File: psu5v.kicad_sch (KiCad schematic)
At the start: 26 parts, among them U16 AP64501SP-13

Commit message: work on control logic
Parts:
- renumbered C50 to C52, C51 to C53, C52 to C54, C53 to C55, C54 to C56, C55 to C57, C56 to C58, C57 to C59, C58 to C60, C59 to C61, C60 to C62, C61 to C63, C62 to C64, C63 to C65, C64 to C66, C65 to C67, R61 to R64, R62 to R65, R63 to R66, R64 to R67, R65 to R68, U16 to U17
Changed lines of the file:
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@@
   (symbol (lib_id "power:GND") (at 152.4 148.59 0) (unit 1)
     (in_bom yes) (on_board yes)
-    (property "Reference" "#PWR049" (id 0) (at 152.4 154.94 0)
+    (property "Reference" "#PWR050" (id 0) (at 152.4 154.94 0)
       (effects (font (size 1.27 1.27)) hide)
     )
@@
   (symbol (lib_id "Device:C_Small") (at 259.08 111.76 0) (unit 1)
     (in_bom yes) (on_board yes)
-    (property "Reference" "C62" (id 0) (at 261.62 110.49 0)
+    (property "Reference" "C64" (id 0) (at 261.62 110.49 0)
       (effects (font (size 1.27 1.27)) (justify left))
     )
@@
   (symbol (lib_id "Device:R_Small") (at 226.06 137.16 0) (unit 1)
     (in_bom yes) (on_board yes)
-    (property "Reference" "R64" (id 0) (at 227.33 135.89 0)
+    (property "Reference" "R67" (id 0) (at 227.33 135.89 0)
       (effects (font (size 1.27 1.27)) (justify left))
     )
@@
   (symbol (lib_id "Device:R_Small") (at 219.71 118.11 0) (unit 1)
     (in_bom yes) (on_board yes)
-    (property "Reference" "R63" (id 0) (at 220.98 116.84 0)
+    (property "Reference" "R66" (id 0) (at 220.98 116.84 0)
       (effects (font (size 1.27 1.27)) (justify left))
     )
@@
   (symbol (lib_id "Device:C_Small") (at 232.41 118.11 0) (unit 1)
     (in_bom no) (on_board no)
-    (property "Reference" "C60" (id 0) (at 234.95 116.84 0)
+    (property "Reference" "C62" (id 0) (at 234.95 116.84 0)
       (effects (font (size 1.27 1.27)) (justify left))
     )
@@
   (symbol (lib_id "Device:C_Small") (at 213.36 140.97 0) (unit 1)
     (in_bom yes) (on_board yes)
-    (property "Reference" "C59" (id 0) (at 215.9 139.7 0)
+    (property "Reference" "C61" (id 0) (at 215.9 139.7 0)
       (effects (font (size 1.27 1.27)) (justify left))
     )
@@
   (symbol (lib_id "Device:R_Small") (at 306.705 112.395 0) (unit 1)
     (in_bom yes) (on_board yes)
-    (property "Reference" "R65" (id 0) (at 309.88 111.125 0))
+    (property "Reference" "R68" (id 0) (at 309.88 111.125 0))
     (property "Value" "1k" (id 1) (at 309.88 113.665 0))
     (property "Footprint" "Resistor_SMD:R_0402_1005Metric" (id 2) (at 306.705 112.395 0)
@@
   (symbol (lib_id "power:GND") (at 290.83 148.59 0) (unit 1)
     (in_bom yes) (on_board yes)
-    (property "Reference" "#PWR053" (id 0) (at 290.83 154.94 0)
+    (property "Reference" "#PWR054" (id 0) (at 290.83 154.94 0)
       (effects (font (size 1.27 1.27)) hide)
     )
@@
   (symbol (lib_id "Regulator_Switching_Diodes:AP64501SP-13") (at 182.88 124.46 0) (unit 1)
     (in_bom yes) (on_board yes)
-    (property "Reference" "U16" (id 0) (at 182.245 114.3 0))
+    (property "Reference" "U17" (id 0) (at 182.245 114.3 0))
     (property "Value" "AP64501SP-13" (id 1) (at 182.88 116.84 0))
     (property "Footprint" "Regulator_Switching_Diodes:SOIC-8-1EP_3.9x4.9mm_P1.27mm_EP2.95x4.9mm_Mask2.71x3.4mm_ThermalVias" (id 2) (at 182.88 149.86 0)
@@
   (symbol (lib_id "Device:C_Small") (at 248.92 111.76 0) (unit 1)
     (in_bom yes) (on_board yes)
-    (property "Reference" "C61" (id 0) (at 251.46 110.49 0)
+    (property "Reference" "C63" (id 0) (at 251.46 110.49 0)
       (effects (font (size 1.27 1.27)) (justify left))
     )
@@
   (symbol (lib_id "power:GND") (at 279.4 148.59 0) (unit 1)
     (in_bom yes) (on_board yes)
-    (property "Reference" "#PWR052" (id 0) (at 279.4 154.94 0)
+    (property "Reference" "#PWR053" (id 0) (at 279.4 154.94 0)
       (effects (font (size 1.27 1.27)) hide)
     )
@@
   (symbol (lib_id "Device:C_Small") (at 163.83 114.3 0) (unit 1)
     (in_bom yes) (on_board yes)
-    (property "Reference" "C56" (id 0) (at 166.37 113.03 0)
+    (property "Reference" "C58" (id 0) (at 166.37 113.03 0)
       (effects (font (size 1.27 1.27)) (justify left))
     )
@@
   (symbol (lib_id "Device:R_Small") (at 173.99 106.68 270) (unit 1)
     (in_bom yes) (on_board yes)
-    (property "Reference" "R61" (id 0) (at 172.72 104.14 90)
+    (property "Reference" "R64" (id 0) (at 172.72 104.14 90)
       (effects (font (size 1.27 1.27)) (justify left))
     )
@@
   (symbol (lib_id "Device:R_Small") (at 213.36 133.35 0) (unit 1)
     (in_bom yes) (on_board yes)
-    (property "Reference" "R62" (id 0) (at 215.9 132.08 0)
+    (property "Reference" "R65" (id 0) (at 215.9 132.08 0)
       (effects (font (size 1.27 1.27)) (justify left))
     )
@@
   (symbol (lib_id "Device:C_Small") (at 279.4 111.76 0) (unit 1)
     (in_bom yes) (on_board yes)
-    (property "Reference" "C64" (id 0) (at 281.94 110.49 0)
+    (property "Reference" "C66" (id 0) (at 281.94 110.49 0)
       (effects (font (size 1.27 1.27)) (justify left))
     )
@@
   (symbol (lib_id "Device:C_Small") (at 172.72 137.16 0) (unit 1)
     (in_bom yes) (on_board yes)
-    (property "Reference" "C57" (id 0) (at 175.26 135.89 0)
+    (property "Reference" "C59" (id 0) (at 175.26 135.89 0)
       (effects (font (size 1.27 1.27)) (justify left))
     )
@@
   (symbol (lib_id "power:GND") (at 226.06 148.59 0) (unit 1)
     (in_bom yes) (on_board yes)
-    (property "Reference" "#PWR050" (id 0) (at 226.06 154.94 0)
+    (property "Reference" "#PWR051" (id 0) (at 226.06 154.94 0)
       (effects (font (size 1.27 1.27)) hide)
     )
@@
   (symbol (lib_id "Device:C_Small") (at 152.4 128.27 0) (unit 1)
     (in_bom yes) (on_board yes)
-    (property "Reference" "C55" (id 0) (at 154.94 127 0)
+    (property "Reference" "C57" (id 0) (at 154.94 127 0)
       (effects (font (size 1.27 1.27)) (justify left))
     )
@@
   (symbol (lib_id "Device:C_Small") (at 91.44 128.27 0) (unit 1)
     (in_bom yes) (on_board yes)
-    (property "Reference" "C51" (id 0) (at 93.98 127 0)
+    (property "Reference" "C53" (id 0) (at 93.98 127 0)
       (effects (font (size 1.27 1.27)) (justify left))
     )
@@
   (symbol (lib_id "Device:C_Small") (at 269.24 111.76 0) (unit 1)
     (in_bom yes) (on_board yes)
-    (property "Reference" "C63" (id 0) (at 271.78 110.49 0)
+    (property "Reference" "C65" (id 0) (at 271.78 110.49 0)
       (effects (font (size 1.27 1.27)) (justify left))
     )
@@
   (symbol (lib_id "power:GND") (at 306.705 148.59 0) (unit 1)
     (in_bom yes) (on_board yes)
-    (property "Reference" "#PWR054" (id 0) (at 306.705 154.94 0)
+    (property "Reference" "#PWR055" (id 0) (at 306.705 154.94 0)
       (effects (font (size 1.27 1.27)) hide)
     )
@@
   (symbol (lib_id "Device:C_Small") (at 76.2 128.27 0) (unit 1)
     (in_bom yes) (on_board yes)
-    (property "Reference" "C50" (id 0) (at 78.74 127 0)
+    (property "Reference" "C52" (id 0) (at 78.74 127 0)
       (effects (font (size 1.27 1.27)) (justify left))
     )
@@
   (symbol (lib_id "power:GND") (at 251.46 142.24 0) (unit 1)
     (in_bom yes) (on_board yes)
-    (property "Reference" "#PWR051" (id 0) (at 251.46 148.59 0)
+    (property "Reference" "#PWR052" (id 0) (at 251.46 148.59 0)
       (effects (font (size 1.27 1.27)) hide)
     )
@@
   (symbol (lib_id "Capacitor_Tantalum_SMD_MyOwn:CP_EIA-7343-31_Kemet-D") (at 290.83 111.76 0) (unit 1)
     (in_bom yes) (on_board yes)
-    (property "Reference" "C65" (id 0) (at 293.37 110.49 0)
+    (property "Reference" "C67" (id 0) (at 293.37 110.49 0)
       (effects (font (size 1.27 1.27)) (justify left))
     )
@@
   (symbol (lib_id "Device:C_Small") (at 121.92 128.27 0) (unit 1)
     (in_bom yes) (on_board yes)
-    (property "Reference" "C53" (id 0) (at 124.46 127 0)
+    (property "Reference" "C55" (id 0) (at 124.46 127 0)
       (effects (font (size 1.27 1.27)) (justify left))
     )
@@
   (symbol (lib_id "Device:C_Small") (at 106.68 128.27 0) (unit 1)
     (in_bom yes) (on_board yes)
-    (property "Reference" "C52" (id 0) (at 109.22 127 0)
+    (property "Reference" "C54" (id 0) (at 109.22 127 0)
       (effects (font (size 1.27 1.27)) (justify left))
     )
@@
   (symbol (lib_id "Device:C_Small") (at 137.16 128.27 0) (unit 1)
     (in_bom yes) (on_board yes)
-    (property "Reference" "C54" (id 0) (at 139.7 127 0)
+    (property "Reference" "C56" (id 0) (at 139.7 127 0)
       (effects (font (size 1.27 1.27)) (justify left))
     )
@@
   (symbol (lib_id "Device:C_Small") (at 201.93 137.16 0) (unit 1)
     (in_bom yes) (on_board yes)
-    (property "Reference" "C58" (id 0) (at 204.47 135.89 0)
-      (effects (font (size 1.27 1.27)) (justify left))
-    )
+    (property "Reference" "C60" (id 0) (at 204.47 135.89 0)
+      (effects (font (size 1.27 1.27)) (justify left))
+    )

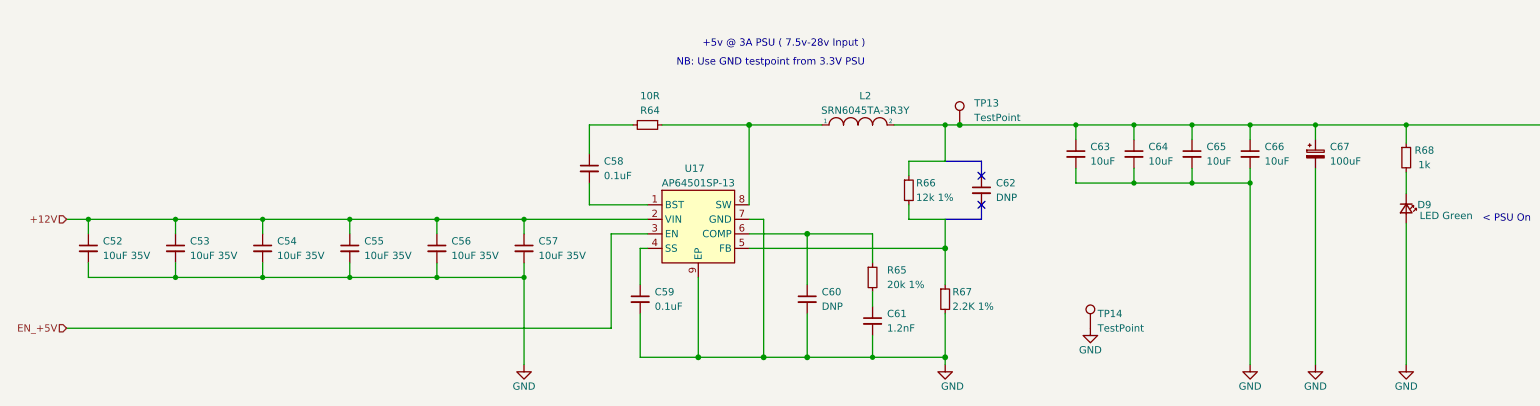
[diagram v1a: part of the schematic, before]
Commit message: connecterized faceplate, refreshed schematic
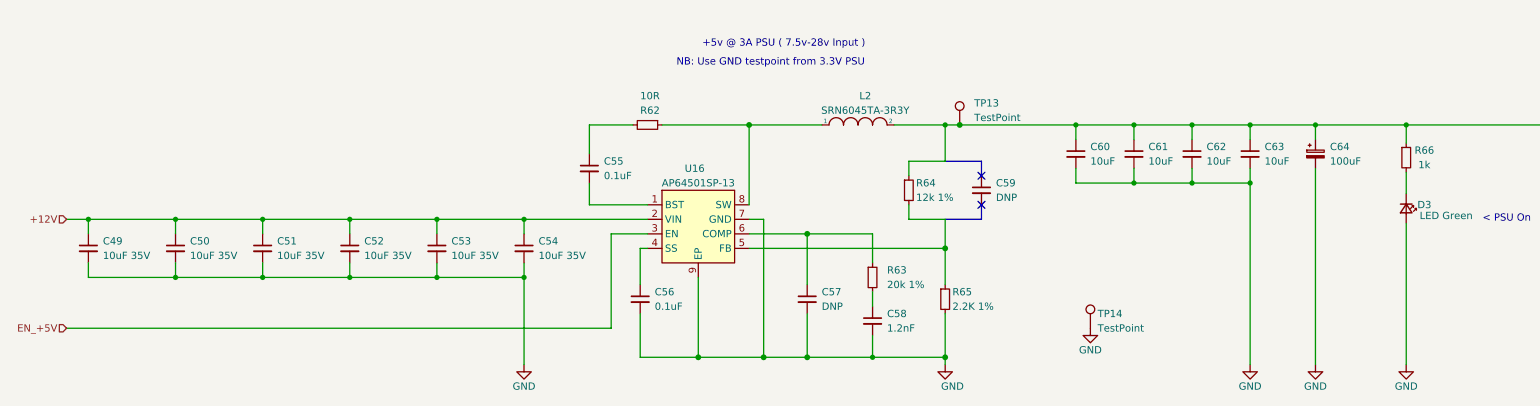
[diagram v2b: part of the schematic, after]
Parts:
- renumbered C52 to C49, C53 to C50, C54 to C51, C55 to C52, C56 to C53, C57 to C54, C58 to C55, C59 to C56, C60 to C57, C61 to C58, C62 to C59, C63 to C60, C64 to C61, C65 to C62, C66 to C63, C67 to C64, D9 to D3, R64 to R62, R65 to R63, R66 to R64, R67 to R65, R68 to R66, U17 to U16
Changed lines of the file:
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@@
   (symbol (lib_id "power:GND") (at 152.4 148.59 0) (unit 1)
     (in_bom yes) (on_board yes)
-    (property "Reference" "#PWR050" (id 0) (at 152.4 154.94 0)
+    (property "Reference" "#PWR049" (id 0) (at 152.4 154.94 0)
       (effects (font (size 1.27 1.27)) hide)
     )
@@
   (symbol (lib_id "Device:C_Small") (at 259.08 111.76 0) (unit 1)
     (in_bom yes) (on_board yes)
-    (property "Reference" "C64" (id 0) (at 261.62 110.49 0)
+    (property "Reference" "C61" (id 0) (at 261.62 110.49 0)
       (effects (font (size 1.27 1.27)) (justify left))
     )
@@
   (symbol (lib_id "Device:R_Small") (at 226.06 137.16 0) (unit 1)
     (in_bom yes) (on_board yes)
-    (property "Reference" "R67" (id 0) (at 227.33 135.89 0)
+    (property "Reference" "R65" (id 0) (at 227.33 135.89 0)
       (effects (font (size 1.27 1.27)) (justify left))
     )
@@
   (symbol (lib_id "Device:R_Small") (at 219.71 118.11 0) (unit 1)
     (in_bom yes) (on_board yes)
-    (property "Reference" "R66" (id 0) (at 220.98 116.84 0)
+    (property "Reference" "R64" (id 0) (at 220.98 116.84 0)
       (effects (font (size 1.27 1.27)) (justify left))
     )
@@
   (symbol (lib_id "Device:C_Small") (at 232.41 118.11 0) (unit 1)
     (in_bom no) (on_board no)
-    (property "Reference" "C62" (id 0) (at 234.95 116.84 0)
+    (property "Reference" "C59" (id 0) (at 234.95 116.84 0)
       (effects (font (size 1.27 1.27)) (justify left))
     )
@@
   (symbol (lib_id "Device:C_Small") (at 213.36 140.97 0) (unit 1)
     (in_bom yes) (on_board yes)
-    (property "Reference" "C61" (id 0) (at 215.9 139.7 0)
+    (property "Reference" "C58" (id 0) (at 215.9 139.7 0)
       (effects (font (size 1.27 1.27)) (justify left))
     )
@@
   (symbol (lib_id "Device:R_Small") (at 306.705 112.395 0) (unit 1)
     (in_bom yes) (on_board yes)
-    (property "Reference" "R68" (id 0) (at 309.88 111.125 0))
+    (property "Reference" "R66" (id 0) (at 309.88 111.125 0))
     (property "Value" "1k" (id 1) (at 309.88 113.665 0))
     (property "Footprint" "Resistor_SMD:R_0402_1005Metric" (id 2) (at 306.705 112.395 0)
@@
   (symbol (lib_id "power:GND") (at 290.83 148.59 0) (unit 1)
     (in_bom yes) (on_board yes)
-    (property "Reference" "#PWR054" (id 0) (at 290.83 154.94 0)
+    (property "Reference" "#PWR053" (id 0) (at 290.83 154.94 0)
       (effects (font (size 1.27 1.27)) hide)
     )
@@
   (symbol (lib_id "Regulator_Switching_Diodes:AP64501SP-13") (at 182.88 124.46 0) (unit 1)
     (in_bom yes) (on_board yes)
-    (property "Reference" "U17" (id 0) (at 182.245 114.3 0))
+    (property "Reference" "U16" (id 0) (at 182.245 114.3 0))
     (property "Value" "AP64501SP-13" (id 1) (at 182.88 116.84 0))
     (property "Footprint" "Regulator_Switching_Diodes:SOIC-8-1EP_3.9x4.9mm_P1.27mm_EP2.95x4.9mm_Mask2.71x3.4mm_ThermalVias" (id 2) (at 182.88 149.86 0)
@@
   (symbol (lib_id "Device:C_Small") (at 248.92 111.76 0) (unit 1)
     (in_bom yes) (on_board yes)
-    (property "Reference" "C63" (id 0) (at 251.46 110.49 0)
+    (property "Reference" "C60" (id 0) (at 251.46 110.49 0)
       (effects (font (size 1.27 1.27)) (justify left))
     )
@@
   (symbol (lib_id "power:GND") (at 279.4 148.59 0) (unit 1)
     (in_bom yes) (on_board yes)
-    (property "Reference" "#PWR053" (id 0) (at 279.4 154.94 0)
+    (property "Reference" "#PWR052" (id 0) (at 279.4 154.94 0)
       (effects (font (size 1.27 1.27)) hide)
     )
@@
   (symbol (lib_id "Device:C_Small") (at 163.83 114.3 0) (unit 1)
     (in_bom yes) (on_board yes)
-    (property "Reference" "C58" (id 0) (at 166.37 113.03 0)
+    (property "Reference" "C55" (id 0) (at 166.37 113.03 0)
       (effects (font (size 1.27 1.27)) (justify left))
     )
@@
   (symbol (lib_id "Device:R_Small") (at 173.99 106.68 270) (unit 1)
     (in_bom yes) (on_board yes)
-    (property "Reference" "R64" (id 0) (at 172.72 104.14 90)
+    (property "Reference" "R62" (id 0) (at 172.72 104.14 90)
       (effects (font (size 1.27 1.27)) (justify left))
     )
@@
   (symbol (lib_id "Device:R_Small") (at 213.36 133.35 0) (unit 1)
     (in_bom yes) (on_board yes)
-    (property "Reference" "R65" (id 0) (at 215.9 132.08 0)
+    (property "Reference" "R63" (id 0) (at 215.9 132.08 0)
       (effects (font (size 1.27 1.27)) (justify left))
     )
@@
   (symbol (lib_id "Device:C_Small") (at 279.4 111.76 0) (unit 1)
     (in_bom yes) (on_board yes)
-    (property "Reference" "C66" (id 0) (at 281.94 110.49 0)
+    (property "Reference" "C63" (id 0) (at 281.94 110.49 0)
       (effects (font (size 1.27 1.27)) (justify left))
     )
@@
   (symbol (lib_id "Device:C_Small") (at 172.72 137.16 0) (unit 1)
     (in_bom yes) (on_board yes)
-    (property "Reference" "C59" (id 0) (at 175.26 135.89 0)
+    (property "Reference" "C56" (id 0) (at 175.26 135.89 0)
       (effects (font (size 1.27 1.27)) (justify left))
     )
@@
   (symbol (lib_id "power:GND") (at 226.06 148.59 0) (unit 1)
     (in_bom yes) (on_board yes)
-    (property "Reference" "#PWR051" (id 0) (at 226.06 154.94 0)
+    (property "Reference" "#PWR050" (id 0) (at 226.06 154.94 0)
       (effects (font (size 1.27 1.27)) hide)
     )
@@
   (symbol (lib_id "Device:C_Small") (at 152.4 128.27 0) (unit 1)
     (in_bom yes) (on_board yes)
-    (property "Reference" "C57" (id 0) (at 154.94 127 0)
+    (property "Reference" "C54" (id 0) (at 154.94 127 0)
       (effects (font (size 1.27 1.27)) (justify left))
     )
@@
   (symbol (lib_id "Device:C_Small") (at 91.44 128.27 0) (unit 1)
     (in_bom yes) (on_board yes)
-    (property "Reference" "C53" (id 0) (at 93.98 127 0)
+    (property "Reference" "C50" (id 0) (at 93.98 127 0)
       (effects (font (size 1.27 1.27)) (justify left))
     )
@@
   (symbol (lib_id "Device:C_Small") (at 269.24 111.76 0) (unit 1)
     (in_bom yes) (on_board yes)
-    (property "Reference" "C65" (id 0) (at 271.78 110.49 0)
+    (property "Reference" "C62" (id 0) (at 271.78 110.49 0)
       (effects (font (size 1.27 1.27)) (justify left))
     )
@@
   (symbol (lib_id "power:GND") (at 306.705 148.59 0) (unit 1)
     (in_bom yes) (on_board yes)
-    (property "Reference" "#PWR055" (id 0) (at 306.705 154.94 0)
+    (property "Reference" "#PWR054" (id 0) (at 306.705 154.94 0)
       (effects (font (size 1.27 1.27)) hide)
     )
@@
   (symbol (lib_id "Device:C_Small") (at 76.2 128.27 0) (unit 1)
     (in_bom yes) (on_board yes)
-    (property "Reference" "C52" (id 0) (at 78.74 127 0)
+    (property "Reference" "C49" (id 0) (at 78.74 127 0)
       (effects (font (size 1.27 1.27)) (justify left))
     )
@@
   (symbol (lib_id "power:GND") (at 251.46 142.24 0) (unit 1)
     (in_bom yes) (on_board yes)
-    (property "Reference" "#PWR052" (id 0) (at 251.46 148.59 0)
+    (property "Reference" "#PWR051" (id 0) (at 251.46 148.59 0)
       (effects (font (size 1.27 1.27)) hide)
     )
@@
   (symbol (lib_id "Capacitor_Tantalum_SMD_MyOwn:CP_EIA-7343-31_Kemet-D") (at 290.83 111.76 0) (unit 1)
     (in_bom yes) (on_board yes)
-    (property "Reference" "C67" (id 0) (at 293.37 110.49 0)
+    (property "Reference" "C64" (id 0) (at 293.37 110.49 0)
       (effects (font (size 1.27 1.27)) (justify left))
     )
@@
   (symbol (lib_id "Device:C_Small") (at 121.92 128.27 0) (unit 1)
     (in_bom yes) (on_board yes)
-    (property "Reference" "C55" (id 0) (at 124.46 127 0)
+    (property "Reference" "C52" (id 0) (at 124.46 127 0)
       (effects (font (size 1.27 1.27)) (justify left))
     )
@@
   (symbol (lib_id "Device:C_Small") (at 106.68 128.27 0) (unit 1)
     (in_bom yes) (on_board yes)
-    (property "Reference" "C54" (id 0) (at 109.22 127 0)
+    (property "Reference" "C51" (id 0) (at 109.22 127 0)
       (effects (font (size 1.27 1.27)) (justify left))
     )
@@
   (symbol (lib_id "Device:C_Small") (at 137.16 128.27 0) (unit 1)
     (in_bom yes) (on_board yes)
-    (property "Reference" "C56" (id 0) (at 139.7 127 0)
+    (property "Reference" "C53" (id 0) (at 139.7 127 0)
       (effects (font (size 1.27 1.27)) (justify left))
     )
@@
   (symbol (lib_id "Device:C_Small") (at 201.93 137.16 0) (unit 1)
     (in_bom yes) (on_board yes)
-    (property "Reference" "C60" (id 0) (at 204.47 135.89 0)
+    (property "Reference" "C57" (id 0) (at 204.47 135.89 0)
       (effects (font (size 1.27 1.27)) (justify left))
     )
@@
   (symbol (lib_id "LED_SMD_LiteOn:LED Green") (at 306.705 121.285 270) (unit 1)
     (in_bom yes) (on_board yes)
-    (property "Reference" "D9" (id 0) (at 309.88 120.65 90))
+    (property "Reference" "D3" (id 0) (at 309.88 120.65 90))
     (property "Value" "LED Green" (id 1) (at 313.69 122.555 90))
     (property "Footprint" "LED_SMD_LiteOn:LED_0603_1608Metric_green" (id 2) (at 296.545 121.285 0)
